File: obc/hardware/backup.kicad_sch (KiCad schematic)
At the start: 24 parts, among them J9 Conn_01x03, Q3 SI7129DN-T1-GE3, U14 TPS564242, U15 TPS564242

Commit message: add user LEDs, fix silkscreen
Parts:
- Q3: LCSC (none) -> C727679
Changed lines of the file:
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@@
+			)
+		)
+		(property "LCSC" "C727679"
+			(at 92.71 66.04 90)
+			(hide yes)
+			(show_name no)
+			(do_not_autoplace no)
+			(effects
+				(font
+					(size 1.27 1.27)
+				)
 			)
 		)

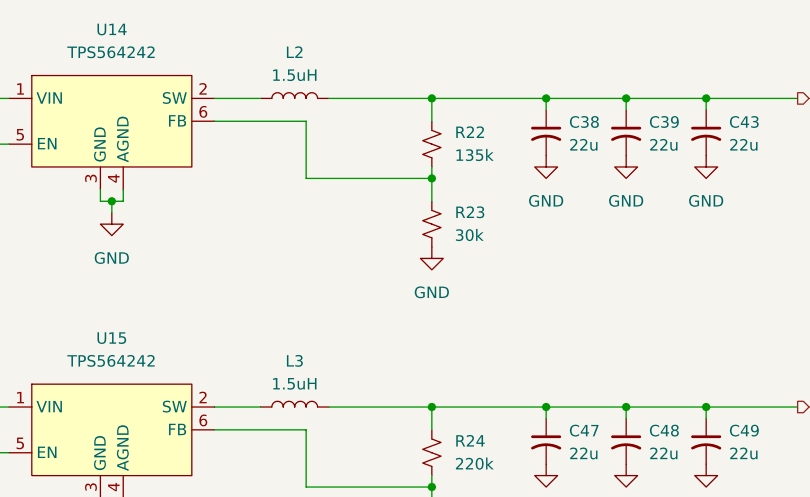
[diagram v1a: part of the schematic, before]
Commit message: swap some pins for better routing, add UART, add more part numbers
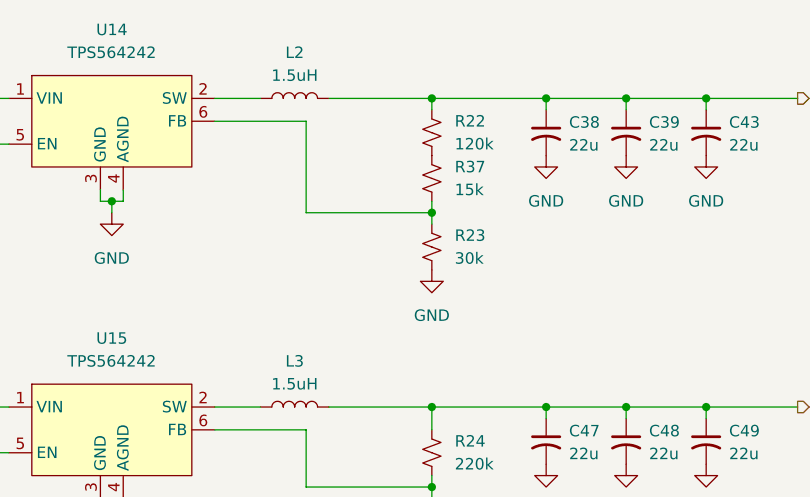
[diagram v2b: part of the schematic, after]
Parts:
- added R37: 15k, Resistor_SMD:R_0402_1005Metric, symbol Device:R_Small_US
- R22: value 135k -> 120k; footprint Resistor_SMD:R_0402_1005Metric -> Resistor_SMD:R_0603_1608Metric; LCSC (none) -> C25808
- R23, R25: footprint Resistor_SMD:R_0402_1005Metric -> Resistor_SMD:R_0603_1608Metric; LCSC (none) -> C22984
- R24: footprint Resistor_SMD:R_0402_1005Metric -> Resistor_SMD:R_0603_1608Metric; LCSC (none) -> C22961
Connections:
- net at R23.1, U14.6 (FB): now also R37.2; no longer R22.2
- new net: R22.2, R37.1
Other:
- moved on the sheet: R22, R23
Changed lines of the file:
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@@
 	)
 	(junction
+		(at 208.28 77.47)
+		(diameter 0)
+		(color 0 0 0 0)
+	)
+	(junction
 		(at 208.28 107.95)
 		(diameter 0)
@@
 	)
 	(junction
-		(at 208.28 64.77)
-		(diameter 0)
-		(color 0 0 0 0)
-	)
-	(junction
 		(at 130.81 99.06)
 		(diameter 0)
@@
 	)
 	(junction
-		(at 208.28 99.06)
+		(at 208.28 64.77)
 		(diameter 0)
 		(color 0 0 0 0)
 	)
 	(junction
-		(at 208.28 73.66)
+		(at 208.28 99.06)
 		(diameter 0)
 		(color 0 0 0 0)
@@
 	(wire
 		(pts
-			(xy 194.31 73.66) (xy 208.28 73.66)
+			(xy 194.31 77.47) (xy 208.28 77.47)
+		)
+		(stroke
+			(width 0)
+			(type default)
+		)
+	)
+	(wire
+		(pts
+			(xy 208.28 77.47) (xy 208.28 78.74)
 		)
 		(stroke
@@
 	(wire
 		(pts
-			(xy 208.28 73.66) (xy 208.28 76.2)
-		)
-		(stroke
-			(width 0)
-			(type default)
-		)
-	)
-	(wire
-		(pts
 			(xy 161.29 64.77) (xy 158.75 64.77)
 		)
@@
 	(wire
 		(pts
-			(xy 208.28 67.31) (xy 208.28 64.77)
+			(xy 208.28 66.04) (xy 208.28 64.77)
 		)
 		(stroke
@@
 	(wire
 		(pts
-			(xy 194.31 67.31) (xy 194.31 73.66)
+			(xy 194.31 67.31) (xy 194.31 77.47)
 		)
 		(stroke
@@
 	(wire
 		(pts
-			(xy 208.28 72.39) (xy 208.28 73.66)
+			(xy 151.13 99.06) (xy 151.13 100.33)
 		)
 		(stroke
@@
 	(wire
 		(pts
-			(xy 151.13 99.06) (xy 151.13 100.33)
+			(xy 229.87 99.06) (xy 229.87 100.33)
 		)
 		(stroke
@@
 	(wire
 		(pts
-			(xy 229.87 99.06) (xy 229.87 100.33)
+			(xy 139.7 99.06) (xy 139.7 100.33)
 		)
 		(stroke
@@
 	(wire
 		(pts
-			(xy 139.7 99.06) (xy 139.7 100.33)
+			(xy 173.99 109.22) (xy 173.99 110.49)
 		)
 		(stroke
@@
 	(wire
 		(pts
-			(xy 173.99 109.22) (xy 173.99 110.49)
+			(xy 208.28 76.2) (xy 208.28 77.47)
 		)
 		(stroke
@@
 	(symbol
 		(lib_id "Device:R_Small_US")
-		(at 208.28 69.85 0)
+		(at 208.28 68.58 0)
 		(unit 1)
 		(body_style 1)
@@
 		(fields_autoplaced yes)
 		(property "Reference" "R22"
-			(at 210.82 68.5799 0)
+			(at 210.82 67.3099 0)
 			(show_name no)
 			(do_not_autoplace no)
@@
 			)
 		)
-		(property "Value" "135k"
-			(at 210.82 71.1199 0)
+		(property "Value" "120k"
+			(at 210.82 69.8499 0)
 			(show_name no)
 			(do_not_autoplace no)
@@
 			)
 		)
-		(property "Footprint" "Resistor_SMD:R_0402_1005Metric"
-			(at 208.28 69.85 0)
+		(property "Footprint" "Resistor_SMD:R_0603_1608Metric"
+			(at 208.28 68.58 0)
 			(hide yes)
 			(show_name no)
@@
 		)
 		(property "Datasheet" ""
-			(at 208.28 69.85 0)
+			(at 208.28 68.58 0)
 			(hide yes)
 			(show_name no)
@@
 		)
 		(property "Description" "Resistor, small US symbol"
-			(at 208.28 69.85 0)
+			(at 208.28 68.58 0)
+			(hide yes)
+			(show_name no)
+			(do_not_autoplace no)
+			(effects
+				(font
+					(size 1.27 1.27)
+				)
+			)
+		)
+		(property "LCSC" "C25808"
+			(at 208.28 68.58 0)
 			(hide yes)
 			(show_name no)
@@
 	)
 	(symbol
+		(lib_id "Device:R_Small_US")
+		(at 208.28 73.66 0)
+		(unit 1)
+		(body_style 1)
+		(exclude_from_sim no)
+		(in_bom yes)
+		(on_board yes)
+		(in_pos_files yes)
+		(dnp no)
+		(fields_autoplaced yes)
+		(property "Reference" "R37"
+			(at 210.82 72.3899 0)
+			(show_name no)
+			(do_not_autoplace no)
+			(effects
+				(font
+					(size 1.27 1.27)
+				)
+				(justify left)
+			)
+		)
+		(property "Value" "15k"
+			(at 210.82 74.9299 0)
+			(show_name no)
+			(do_not_autoplace no)
+			(effects
+				(font
+					(size 1.27 1.27)
+				)
+				(justify left)
+			)
+		)
+		(property "Footprint" "Resistor_SMD:R_0402_1005Metric"
+			(at 208.28 73.66 0)
+			(hide yes)
+			(show_name no)
+			(do_not_autoplace no)
+			(effects
+				(font
+					(size 1.27 1.27)
+				)
+			)
+		)
+		(property "Datasheet" ""
+			(at 208.28 73.66 0)
+			(hide yes)
+			(show_name no)
+			(do_not_autoplace no)
+			(effects
+				(font
+					(size 1.27 1.27)
+				)
+			)
+		)
+		(property "Description" "Resistor, small US symbol"
+			(at 208.28 73.66 0)
+			(hide yes)
+			(show_name no)
+			(do_not_autoplace no)
+			(effects
+				(font
+					(size 1.27 1.27)
+				)
+			)
+		)
+		(property "LCSC" "C25756"
+			(at 208.28 73.66 0)
+			(hide yes)
+			(show_name no)
+			(do_not_autoplace no)
+			(effects
+				(font
+					(size 1.27 1.27)
+				)
+			)
+		)
+		(pin "1"
+		)
+		(pin "2"
+		)
+		(instances
+			(project "obc"
+				(path "/ba4f88ff-24aa-49a3-8871-8c7e48b371c5/76b49e78-dec3-4db8-80be-7d93a848591c"
+					(reference "R37")
+					(unit 1)
+				)
+			)
+		)
+	)
+	(symbol
 		(lib_id "obc-symbols:TPS56424x")
 		(at 172.72 67.31 0)
@@
 	(symbol
 		(lib_id "Device:R_Small_US")
-		(at 208.28 78.74 0)
+		(at 208.28 81.28 0)
 		(unit 1)
 		(body_style 1)
@@
 		(fields_autoplaced yes)
 		(property "Reference" "R23"
-			(at 210.82 77.4699 0)
+			(at 210.82 80.0099 0)
 			(show_name no)
 			(do_not_autoplace no)
@@
 		)
 		(property "Value" "30k"
-			(at 210.82 80.0099 0)
+			(at 210.82 82.5499 0)
 			(show_name no)
 			(do_not_autoplace no)
@@
 			)
 		)
-		(property "Footprint" "Resistor_SMD:R_0402_1005Metric"
-			(at 208.28 78.74 0)
+		(property "Footprint" "Resistor_SMD:R_0603_1608Metric"
+			(at 208.28 81.28 0)
 			(hide yes)
 			(show_name no)
@@
 		)
 		(property "Datasheet" ""
-			(at 208.28 78.74 0)
+			(at 208.28 81.28 0)
 			(hide yes)
 			(show_name no)
@@
 		)
 		(property "Description" "Resistor, small US symbol"
-			(at 208.28 78.74 0)
+			(at 208.28 81.28 0)
+			(hide yes)
+			(show_name no)
+			(do_not_autoplace no)
+			(effects
+				(font
+					(size 1.27 1.27)
+				)
+			)
+		)
+		(property "LCSC" "C22984"
+			(at 208.28 81.28 0)
 			(hide yes)
 			(show_name no)
@@
 	(symbol
 		(lib_id "power:GND")
-		(at 208.28 81.28 0)
+		(at 208.28 83.82 0)
 		(unit 1)
 		(body_style 1)
@@
 		(fields_autoplaced yes)
 		(property "Reference" "#PWR093"
-			(at 208.28 87.63 0)
+			(at 208.28 90.17 0)
 			(hide yes)
 			(show_name no)
@@
 		)
 		(property "Value" "GND"
-			(at 208.28 86.36 0)
+			(at 208.28 88.9 0)
 			(show_name no)
 			(do_not_autoplace no)
@@
 		)
 		(property "Footprint" ""
-			(at 208.28 81.28 0)
+			(at 208.28 83.82 0)
 			(hide yes)
 			(show_name no)
@@
 		)
 		(property "Datasheet" ""
-			(at 208.28 81.28 0)
+			(at 208.28 83.82 0)
 			(hide yes)
 			(show_name no)
@@
 		)
 		(property "Description" "Power symbol creates a global label with name \"GND\" , ground"
-			(at 208.28 81.28 0)
+			(at 208.28 83.82 0)
 			(hide yes)
 			(show_name no)
@@
 			)
 		)
-		(property "Footprint" "Resistor_SMD:R_0402_1005Metric"
+		(property "Footprint" "Resistor_SMD:R_0603_1608Metric"
 			(at 208.28 104.14 0)
 			(hide yes)
@@
 			)
 		)
+		(property "LCSC" "C22961"
+			(at 208.28 104.14 0)
+			(hide yes)
+			(show_name no)
+			(do_not_autoplace no)
+			(effects
+				(font
+					(size 1.27 1.27)
+				)
+			)
+		)
 		(pin "1"
 		)
@@
 			)
 		)
-		(property "Footprint" "Resistor_SMD:R_0402_1005Metric"
+		(property "Footprint" "Resistor_SMD:R_0603_1608Metric"
 			(at 208.28 113.03 0)
 			(hide yes)
@@
 			(at 208.28 113.03 0)
 			(hide yes)
+			(show_name no)
+			(do_not_autoplace no)
+			(effects
+				(font
+					(size 1.27 1.27)
+				)
+			)
+		)
+		(property "LCSC" "C22984"
+			(at 208.28 113.03 0)
+			(hide yes)

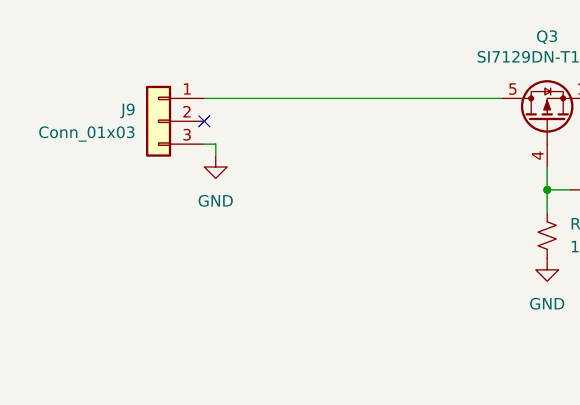
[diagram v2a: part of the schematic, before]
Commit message: DNP parts that JLC shouldn't assemble
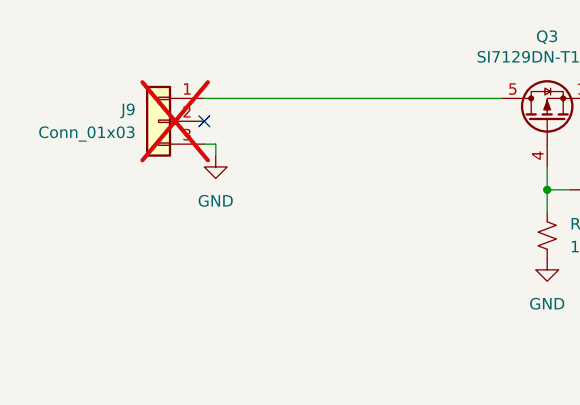
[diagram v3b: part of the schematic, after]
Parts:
- J9: now not fitted
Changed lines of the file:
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@@
 		(on_board yes)
 		(in_pos_files yes)
-		(dnp no)
+		(dnp yes)
 		(property "Reference" "J9"
 			(at 46.99 66.0399 0)
